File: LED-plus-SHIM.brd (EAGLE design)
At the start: 56 x 65 mm, 305 parts, among them IC1 TXB0101DCKR

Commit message: Fixed some texts
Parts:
- moved LOGO3 12.3 mm to (32.7, 45.9)
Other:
- board text added: "LED-plus-SHIM v1.0"
- board text removed: "LED-zero-SHIM v1.0"
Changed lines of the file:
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@@
 <wire x1="0" y1="2.9972" x2="0" y2="3" width="0" layer="20" curve="-0.053476"/>
 <wire x1="0" y1="62" x2="0" y2="62.0014" width="0" layer="20" curve="-0.026738"/>
-<text x="47.191" y="42.83" size="1.27" layer="22" font="vector" ratio="24" rot="MR0">LED-zero-SHIM v1.0</text>
-<text x="45.011" y="49.307" size="1.016" layer="22" font="vector" ratio="12" rot="MR0">http://redscorp.net</text>
-<text x="45.011" y="48.037" size="1.016" layer="22" font="vector" ratio="12" rot="MR0">(c) Andriy Golovnya</text>
+<text x="36.142" y="37.496" size="1.27" layer="22" font="vector" ratio="24" rot="MR0">LED-plus-SHIM v1.0</text>
+<text x="33.962" y="43.973" size="1.016" layer="22" font="vector" ratio="12" rot="MR0">http://redscorp.net</text>
+<text x="33.962" y="42.703" size="1.016" layer="22" font="vector" ratio="12" rot="MR0">(c) Andriy Golovnya</text>
 <wire x1="0" y1="2.9972" x2="0" y2="62.0014" width="0" layer="20"/>
 <text x="48.26" y="64.008" size="0.8128" layer="22" font="vector" rot="MR0">GPIO21</text>
@@
 <elements>
 <element name="LOGO1" library="_my_logos" package="MFDEC_L_30MM" value="MFDECLOGO_L_30MM" x="-4.191" y="-7.112" smashed="yes" rot="MR90"/>
-<element name="LOGO3" library="_my_logos" package="RSNURL_QR_10MM" value="RSNURL_QR_10MM" x="43.741" y="51.212" smashed="yes" rot="MR0"/>
+<element name="LOGO3" library="_my_logos" package="RSNURL_QR_10MM" value="RSNURL_QR_10MM" x="32.692" y="45.878" smashed="yes" rot="MR0"/>
 <element name="LED2" library="WS281X" package="WS2812X-2020" value="WS2812C-2020" x="47.752" y="53.34" smashed="yes" rot="R270">
 <attribute name="NAME" x="49.022" y="54.61" size="0.6096" layer="27" font="vector" rot="R270"/>

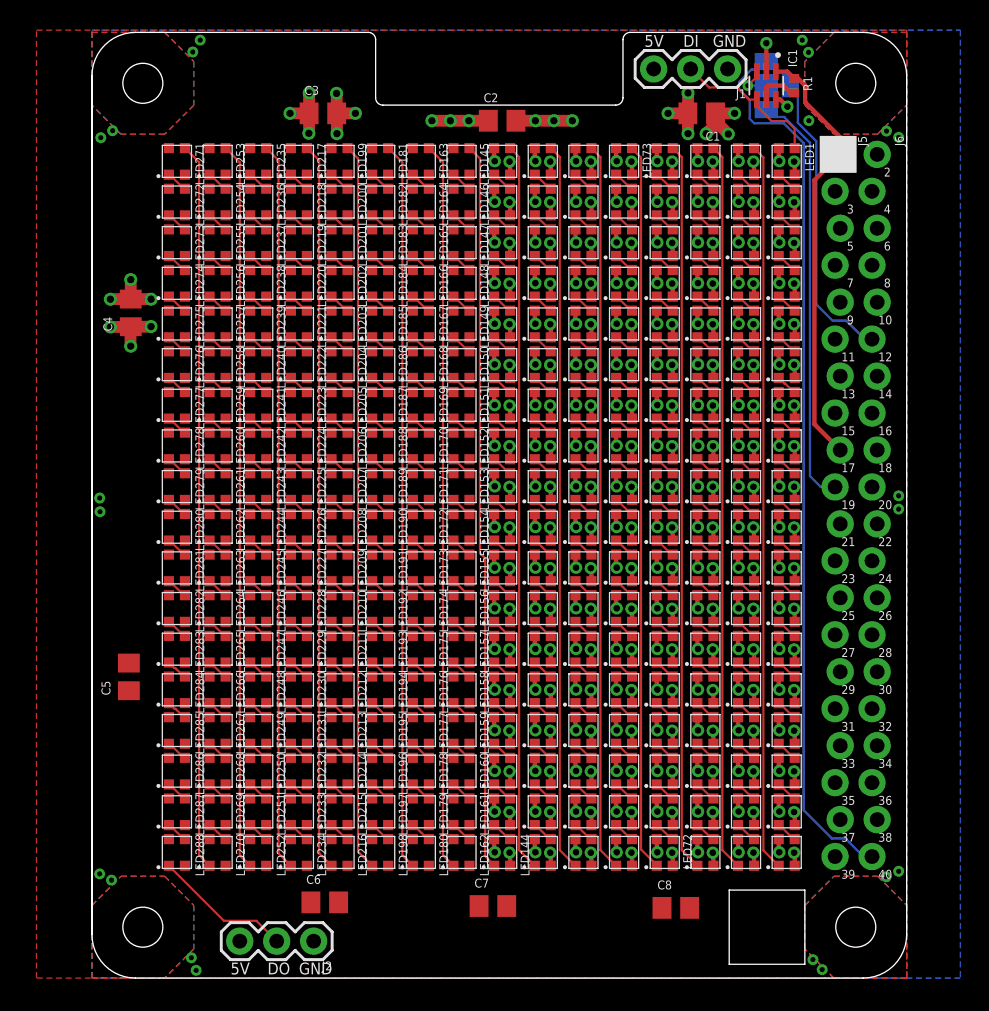
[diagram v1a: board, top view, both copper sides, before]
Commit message: Finished tracing plus SHIM board.
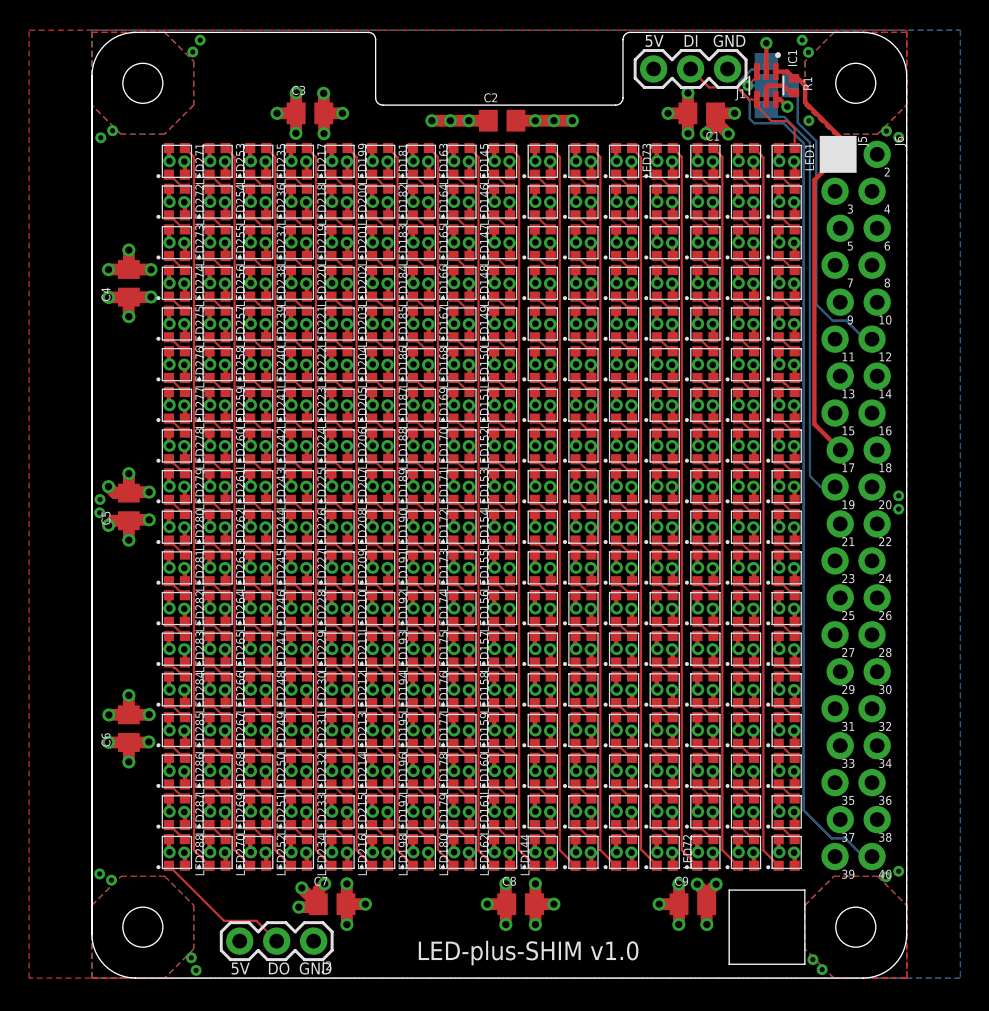
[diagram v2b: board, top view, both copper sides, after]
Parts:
- added C9: 10uF, rcl:C0805
- LOGO1: value MFDECLOGO_L_30MM -> MFDECLOGO_L_40MM; device _my_logos:MFDEC_L_30MM -> _my_logos:MFDEC_L_40MM
- moved C6 18.0 mm to (2.54, 17.1), turned to 90 degrees
- moved C5 11.7 mm to (2.54, 32.4)
- moved C7 11.0 mm to (16.5, 5.08)
- moved C8 10.7 mm to (29.5, 5.08)
- moved LOGO1 3.96 mm to (-1.52, -10.0)
- moved LOGO3 2.65 mm to (33.5, 48.4)
- moved C4 2.04 mm to (2.54, 47.8)
- moved C3 0.89 mm to (15.0, 59.4)
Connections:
- net 5V: now also C9.1
- net GND: now also C9.2
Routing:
- net GND: track 150.4 -> 304.2 mm, vias 168 -> 327
- net 5V: track 149.9 -> 303.5 mm, vias 167 -> 326

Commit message: Moved few traces around.
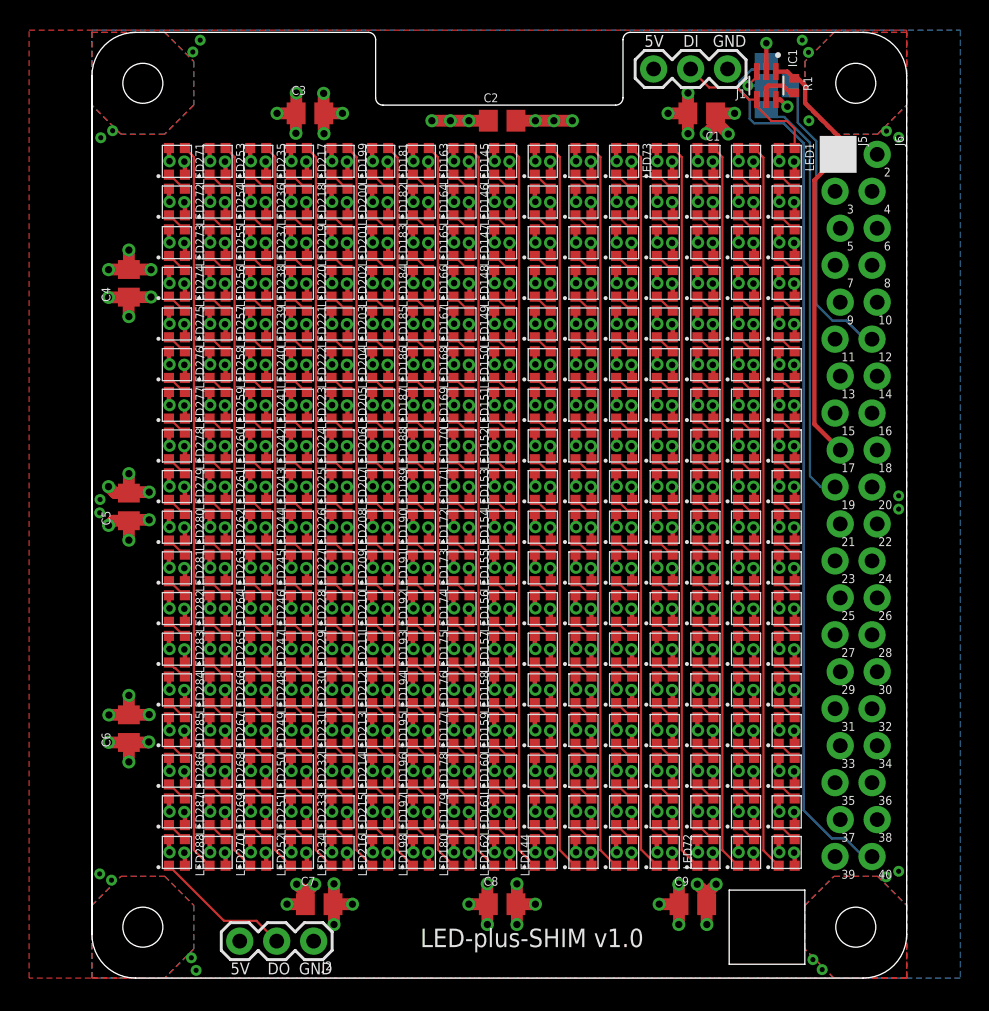
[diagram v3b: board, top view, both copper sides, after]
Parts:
- moved C8 1.27 mm to (28.2, 5.08)
- moved C7 0.89 mm to (15.6, 5.08)

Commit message: Added few vias
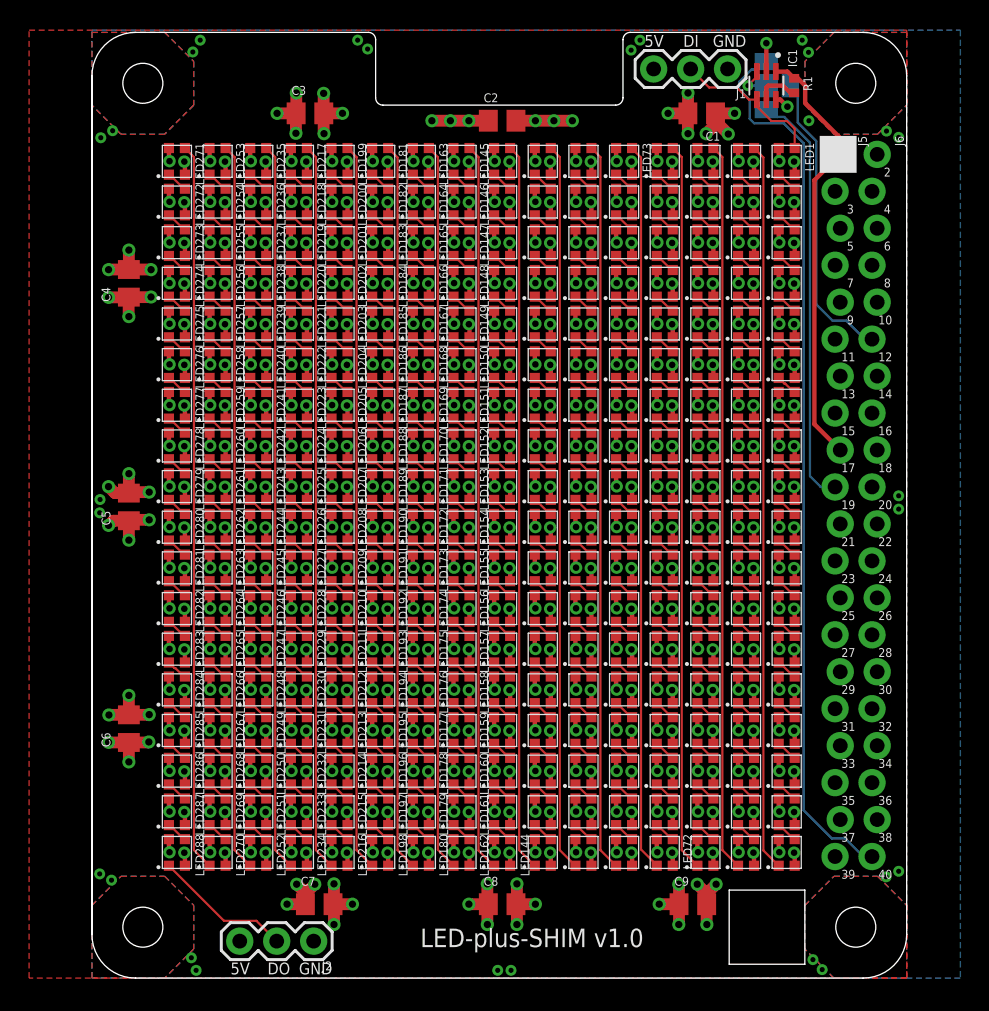
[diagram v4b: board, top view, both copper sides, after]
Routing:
- net GND: vias 327 -> 330
- net 5V: vias 326 -> 329
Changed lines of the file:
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@@
 <wire x1="15.9258" y1="58.0644" x2="15.9258" y2="59.4462" width="0.8128" layer="1"/>
 <wire x1="30.48" y1="58.928" x2="29.144" y2="58.928" width="0.8128" layer="1"/>
+<via x="27.8892" y="0.5334" extent="1-16" drill="0.35"/>
+<via x="18.9484" y="63.8556" extent="1-16" drill="0.35"/>
+<via x="37.0586" y="63.7794" extent="1-16" drill="0.35"/>
 </signal>
 <signal name="3.3V">
@@
 <wire x1="14.0716" y1="6.4516" x2="14.671" y2="5.8522" width="0.8128" layer="1"/>
 <wire x1="14.671" y1="5.8522" x2="14.671" y2="5.08" width="0.8128" layer="1"/>
+<via x="28.8036" y="0.5334" extent="1-16" drill="0.35"/>
+<via x="18.2626" y="64.4652" extent="1-16" drill="0.35"/>
+<via x="37.6682" y="64.4652" extent="1-16" drill="0.35"/>
 </signal>
 <signal name="N$1">
